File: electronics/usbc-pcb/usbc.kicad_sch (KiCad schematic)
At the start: 4 parts, among them J1 USB4736-GF-A, J2 To joystick PCB

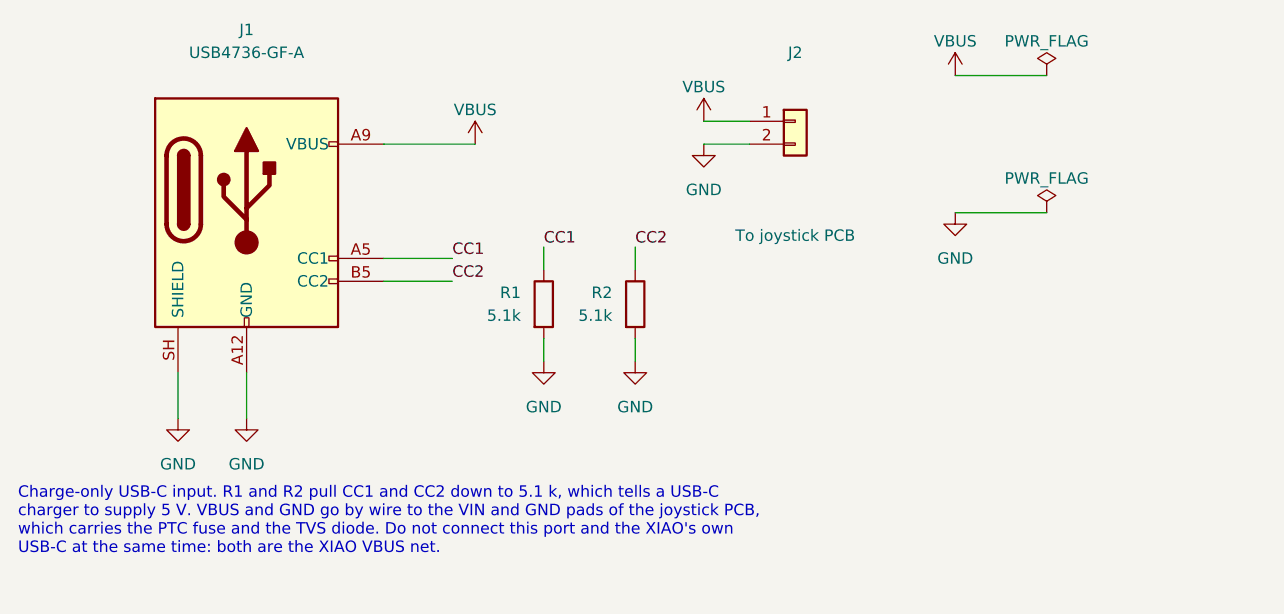
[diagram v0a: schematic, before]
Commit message: Add a charge LED beside the V0.24 charging port
Put a red side-looking LED (Lite-On LTST-S270KRKT) on the USB-C PCB,
at its front edge beside the receptacle, with a 1 k resistor and a wire
pad to XIAO D8. The board grows from 14 to 19 mm wide to carry it. The
housing gets a 1.6 mm window through the panel on the LED axis, filled
with clear epoxy, clear of the gasket pocket and the plug overmold.

The charger's CHG signal reaches no XIAO pad, so the firmware copies it
to D8: the LED is on while the cell charges and off otherwise. Specify
the power behaviour: no power switch, A + B + C held 3 s to turn off,
auto-off after 6 h without input, wake on any button or on plugging in
a charger.

Signed-off-by: Marc Cirauqui <marc@tetrate.io>
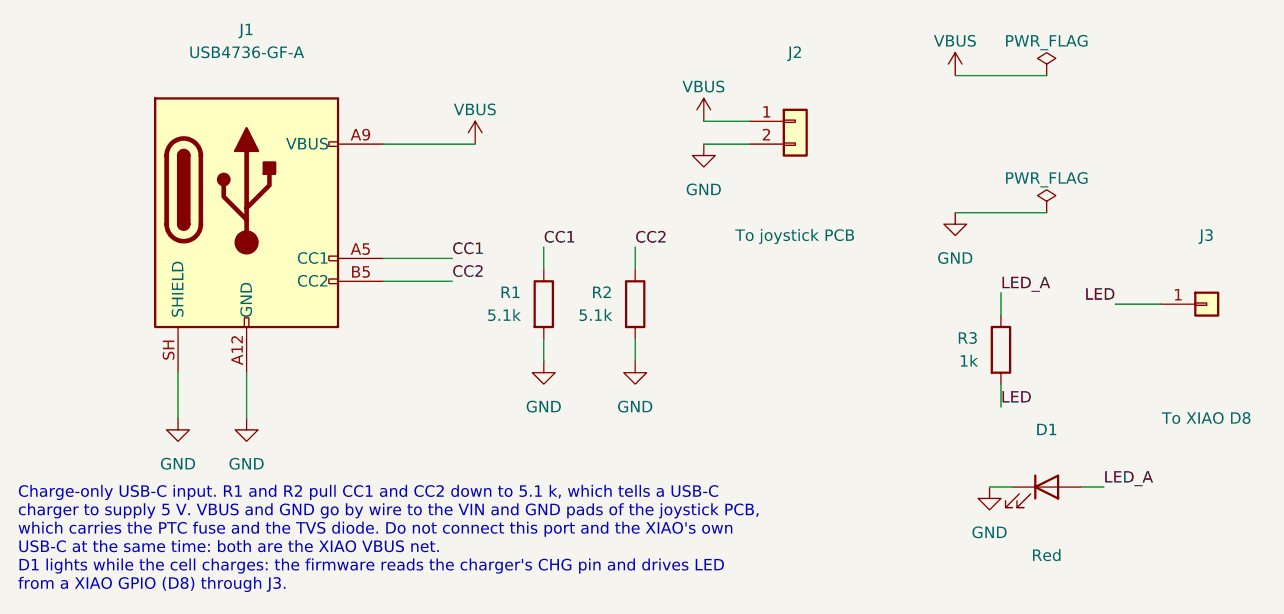
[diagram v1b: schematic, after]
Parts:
- added D1: Red, orr:LED_LiteOn_LTST-S270, symbol Device:LED
- added J3: To XIAO D8, orr:WirePad_1x01, symbol Connector_Generic:Conn_01x01
- added R3: 1k, Resistor_SMD:R_0603_1608Metric, symbol Device:R
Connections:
- net GND: now also D1.1 (K)
- new net LED: J3.1 (Pin_1), R3.2
- new net LED_A: D1.2 (A), R3.1
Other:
- note added: "Charge-only USB-C input. R1 and R2 pull CC1 and CC2 down to 5.1 k, which tells a USB-C charger to supply 5 V. VBUS and GND go by wire to the VIN and GND pads of the joystick PCB, which carries the PTC fuse and the TVS diode. Do not connect this port and the XIAO's own USB-C at the same time: both are the XIAO VBUS net. D1 lights while the cell charges: the firmware reads the charger's CHG pin and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"
- note removed: "Charge-only USB-C input. R1 and R2 pull CC1 and CC2 down to 5.1 k, which tells a USB-C charger to supply 5 V. VBUS and GND go by wire to the VIN and GND pads of the joystick PCB, which carries the PTC fuse and the TVS diode. Do not connect this port and the XIAO's own USB-C at the same time: both are the XIAO VBUS net."
